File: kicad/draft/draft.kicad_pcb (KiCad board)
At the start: 2 copper layers, 15 parts, among them IC1 LP5024RSMR, J1 Conn_02x05_Odd_Even, U1 NodeMCU2

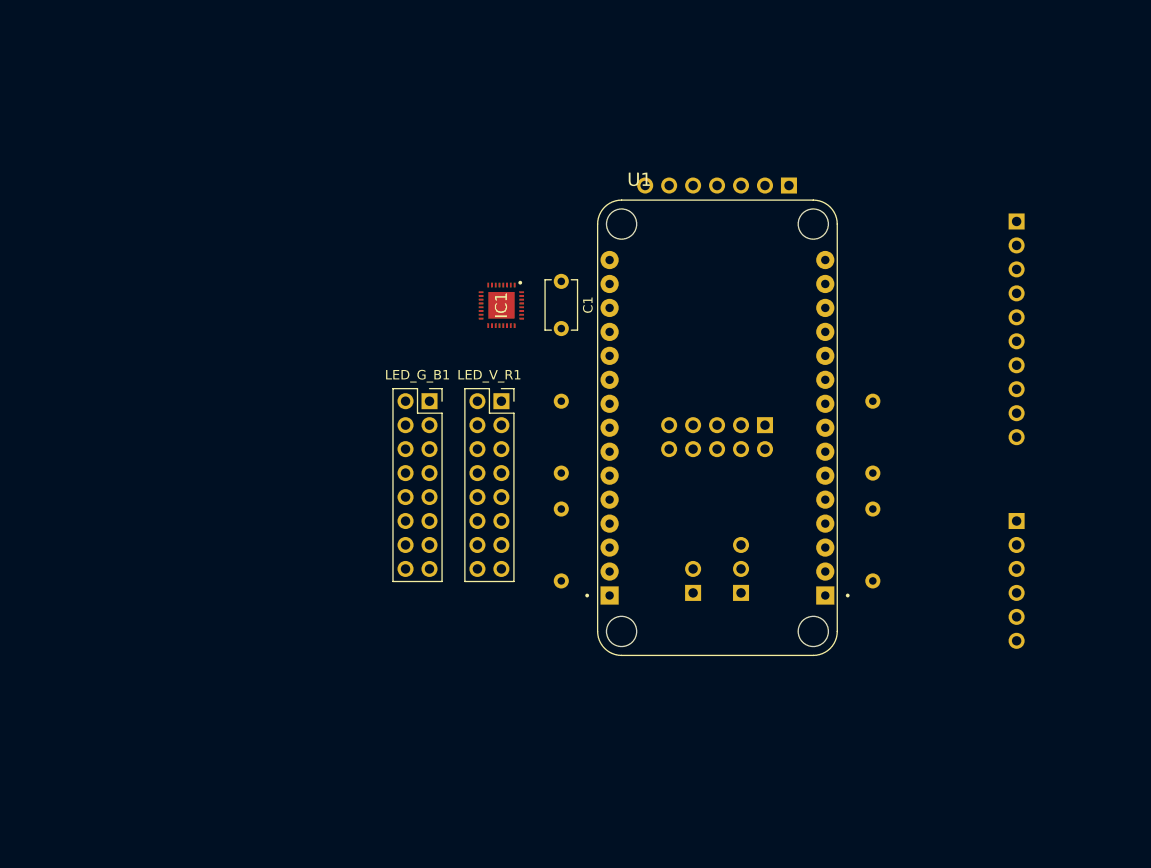
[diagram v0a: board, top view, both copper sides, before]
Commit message: Added GND and 3V3 areas and tracks to connect NodeMCU
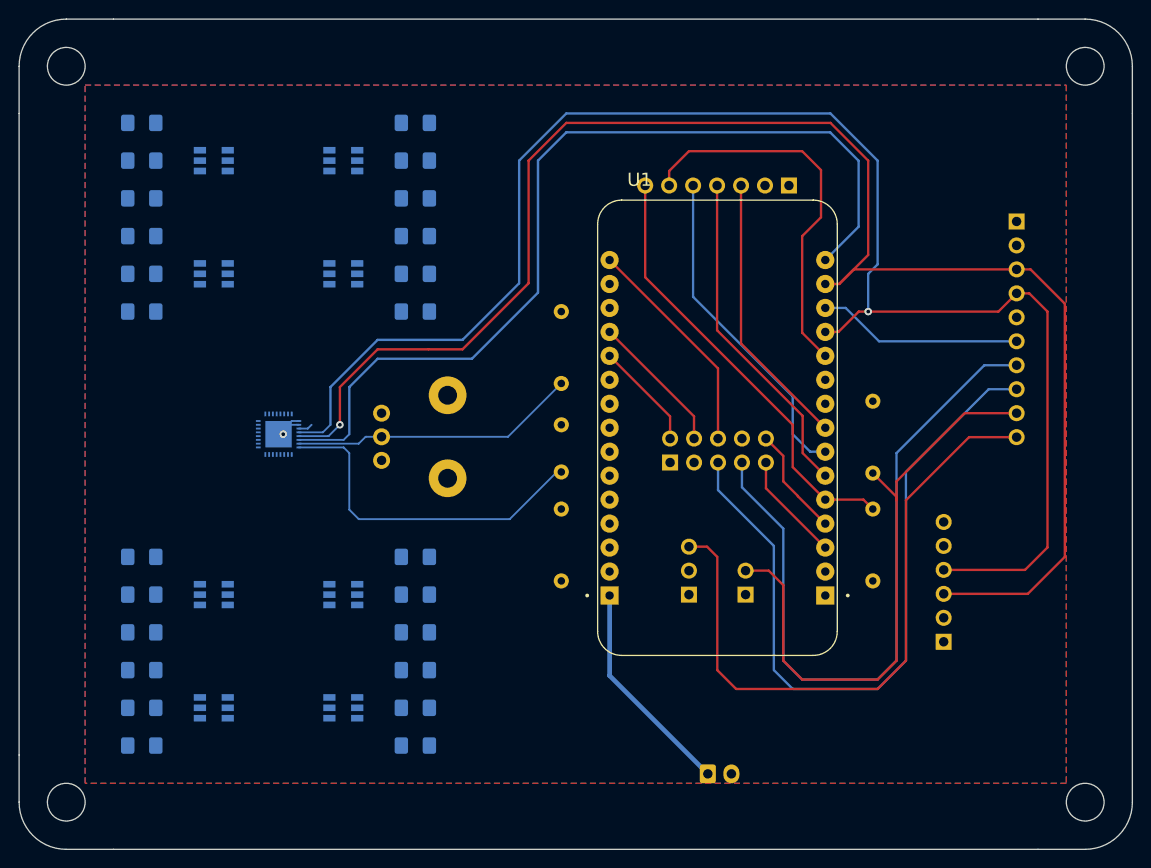
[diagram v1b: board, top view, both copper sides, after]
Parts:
- removed LED_G_B1: LED_G_B, Connector_PinSocket_2.54mm:PinSocket_2x08_P2.54mm_Vertical
- removed LED_V_R1: LED_V_R, Connector_PinSocket_2.54mm:PinSocket_2x08_P2.54mm_Vertical
- added J2: Conn_01x02_Female, Connector_JST:JST_EH_S2B-EH_1x02_P2.50mm_Horizontal, B.Cu at (93.0, 103.0)
- added LED1: LED, SamacSys:KRTBLSLPS132VUVXEQBTBVD8TWTZL1B, B.Cu at (40.6, 38.0)
- added LED2: LED, SamacSys:KRTBLSLPS132VUVXEQBTBVD8TWTZL1B, B.Cu at (40.6, 84.0)
- added LED3: LED, SamacSys:KRTBLSLPS132VUVXEQBTBVD8TWTZL1B, B.Cu at (40.6, 50.0)
- added LED4: LED, SamacSys:KRTBLSLPS132VUVXEQBTBVD8TWTZL1B, B.Cu at (40.6, 96.0)
- added LED5: LED, SamacSys:KRTBLSLPS132VUVXEQBTBVD8TWTZL1B, B.Cu at (54.4, 38.0)
- added LED6: LED, SamacSys:KRTBLSLPS132VUVXEQBTBVD8TWTZL1B, B.Cu at (54.4, 84.0)
- added LED7: LED, SamacSys:KRTBLSLPS132VUVXEQBTBVD8TWTZL1B, B.Cu at (54.4, 50.0)
- added LED8: LED, SamacSys:KRTBLSLPS132VUVXEQBTBVD8TWTZL1B, B.Cu at (54.4, 96.0)
- added R10: 47, Resistor_SMD:R_1206_3216Metric_Pad1.42x1.75mm_HandSolder, B.Cu at (33.0, 92.0)
- added R11: 47, Resistor_SMD:R_1206_3216Metric_Pad1.42x1.75mm_HandSolder, B.Cu at (33.0, 96.0)
- added R12: 100, Resistor_SMD:R_1206_3216Metric_Pad1.42x1.75mm_HandSolder, B.Cu at (33.0, 54.0)
- added R13: 100, Resistor_SMD:R_1206_3216Metric_Pad1.42x1.75mm_HandSolder, B.Cu at (33.0, 100.0)
- added R14: 47, Resistor_SMD:R_1206_3216Metric_Pad1.42x1.75mm_HandSolder, B.Cu at (33.0, 50.0)
- added R15: 47, Resistor_SMD:R_1206_3216Metric_Pad1.42x1.75mm_HandSolder, B.Cu at (33.0, 46.0)
- added R16: 47, Resistor_SMD:R_1206_3216Metric_Pad1.42x1.75mm_HandSolder, B.Cu at (62.0, 88.0)
- added R17: 47, Resistor_SMD:R_1206_3216Metric_Pad1.42x1.75mm_HandSolder, B.Cu at (62.0, 84.0)
- added R18: 100, Resistor_SMD:R_1206_3216Metric_Pad1.42x1.75mm_HandSolder, B.Cu at (62.0, 34.0)
- added R19: 100, Resistor_SMD:R_1206_3216Metric_Pad1.42x1.75mm_HandSolder, B.Cu at (62.0, 80.0)
- added R20: 47, Resistor_SMD:R_1206_3216Metric_Pad1.42x1.75mm_HandSolder, B.Cu at (62.0, 38.0)
- added R21: 47, Resistor_SMD:R_1206_3216Metric_Pad1.42x1.75mm_HandSolder, B.Cu at (62.0, 42.0)
- added R22: 47, Resistor_SMD:R_1206_3216Metric_Pad1.42x1.75mm_HandSolder, B.Cu at (62.0, 100.0)
- added R23: 47, Resistor_SMD:R_1206_3216Metric_Pad1.42x1.75mm_HandSolder, B.Cu at (62.0, 96.0)
- added R24: 100, Resistor_SMD:R_1206_3216Metric_Pad1.42x1.75mm_HandSolder, B.Cu at (62.0, 46.0)
- added R25: 100, Resistor_SMD:R_1206_3216Metric_Pad1.42x1.75mm_HandSolder, B.Cu at (62.0, 92.0)
- added R26: 47, Resistor_SMD:R_1206_3216Metric_Pad1.42x1.75mm_HandSolder, B.Cu at (62.0, 50.0)
- added R27: 47, Resistor_SMD:R_1206_3216Metric_Pad1.42x1.75mm_HandSolder, B.Cu at (62.0, 54.0)
- added R4: 47, Resistor_SMD:R_1206_3216Metric_Pad1.42x1.75mm_HandSolder, B.Cu at (33.0, 80.0)
- added R5: 47, Resistor_SMD:R_1206_3216Metric_Pad1.42x1.75mm_HandSolder, B.Cu at (33.0, 84.0)
- added R6: 100, Resistor_SMD:R_1206_3216Metric_Pad1.42x1.75mm_HandSolder, B.Cu at (33.0, 42.0)
- added R7: 100, Resistor_SMD:R_1206_3216Metric_Pad1.42x1.75mm_HandSolder, B.Cu at (33.0, 88.0)
- added R8: 47, Resistor_SMD:R_1206_3216Metric_Pad1.42x1.75mm_HandSolder, B.Cu at (33.0, 38.0)
- added R9: 47, Resistor_SMD:R_1206_3216Metric_Pad1.42x1.75mm_HandSolder, B.Cu at (33.0, 34.0)
- added RV1: R_POT 5K (for 15mA LED), Potentiometer_THT:Potentiometer_Bourns_PTV09A-1_Single_Vertical, B.Cu at (58.4, 64.8)
- C1, IC1: moved to B.Cu
- moved IC1 27.3 mm to (47.5, 67.0), turned to 90 degrees
- moved C1 20.2 mm to (77.5, 71.0), turned to 90 degrees
- moved R5 17.1 mm to (77.5, 54.0), turned to 270 degrees
- moved BME1 15.0 mm to (118.0, 89.0), turned to 0 degrees
- moved J1 10.8 mm to (89.0, 70.0), turned to 270 degrees
- moved R3 5.56 mm to (97.0, 84.0)
- moved MOIST1 5.52 mm to (91.0, 84.0)
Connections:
- ADC1 pad 10: (no net) -> Net-(ADC1-Pad10)
- ADC1 pad 5: Net-(ADC1-Pad5) -> GND
- C1 pad 1: GND -> Net-(C1-Pad1)
- C1 pad 2: Net-(C1-Pad2) -> GND
- IC1 pad 32: Net-(C1-Pad2) -> Net-(C1-Pad1)
- J1 pad 2: GND -> Net-(J1-Pad2)
- J1 pad 3: Net-(J1-Pad3) -> GND
- J1 pad 5: Net-(J1-Pad5) -> Net-(ADC1-Pad8)
- J1 pad 7: Net-(J1-Pad7) -> Net-(ADC1-Pad7)
- MOIST1 pad 3: Net-(ADC1-Pad6) -> Net-(ADC1-Pad10)
- R2 pad 1: Net-(ADC1-Pad7) -> Net-(ADC1-Pad9)
- R3 pad 2: Net-(ADC1-Pad7) -> Net-(ADC1-Pad9)
- U1 pad A0: Net-(J1-Pad7) -> Net-(J1-Pad6)
- U1 pad D0: Net-(J1-Pad10) -> Net-(IC1-Pad30)
- U1 pad D10: Net-(J1-Pad4) -> Net-(J1-Pad9)
- U1 pad D2: Net-(J1-Pad8) -> Net-(ADC1-Pad6)
- U1 pad D9: Net-(J1-Pad6) -> Net-(J1-Pad10)
- U1 pad SD2: Net-(J1-Pad3) -> Net-(J1-Pad2)
- U1 pad SD3: Net-(J1-Pad5) -> Net-(J1-Pad4)
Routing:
- net Net-(ADC1-Pad3): track 0.00 -> 168.9 mm, vias 0 -> 1
- net Net-(ADC1-Pad4): track 0.00 -> 166.8 mm, vias 0 -> 1
- net Net-(IC1-Pad30): track 0.00 -> 97.2 mm
- net Net-(ADC1-Pad8): track 0.00 -> 75.9 mm
- net Net-(ADC1-Pad7): track 0.00 -> 75.1 mm
- net Net-(ADC1-Pad10): track 0.00 -> 69.0 mm
- net Net-(ADC1-Pad9): track 0.00 -> 65.5 mm
- net Net-(LCD_SPI1-Pad7): track 0.00 -> 46.7 mm
- net Net-(LCD_SPI1-Pad6): track 0.00 -> 40.9 mm
- net Net-(C1-Pad1): track 0.00 -> 36.6 mm
- net Net-(LCD_SPI1-Pad4): track 0.00 -> 35.5 mm
- net Net-(LCD_SPI1-Pad5): track 0.00 -> 35.0 mm
- net Net-(IC1-Pad31): track 0.00 -> 30.5 mm
- net Net-(LCD_SPI1-Pad3): track 0.00 -> 29.4 mm
- net Net-(J1-Pad6): track 0.00 -> 23.7 mm
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- added copper zone on B.Cu, net +3V3
- added copper zone on F.Cu, net GND
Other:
- board outline added: 118 x 88 mm
- net class IC_LD_OUT added: clearance 0.1, trace_width 0.2, via_dia 0.8, via_drill 0.4

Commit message: PCB 0.1 sent to production
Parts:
- removed the R4 at (33.0, 80.0)
- removed the R4 at (77.5, 82.5)
- removed the R5 at (33.0, 84.0)
- removed the R5 at (77.5, 54.0)
- added C2: 1μF, Capacitor_SMD:C_1206_3216Metric_Pad1.42x1.75mm_HandSolder, B.Cu at (59.1, 62.2)
- added R4: 47, Resistor_SMD:R_1206_3216Metric_Pad1.42x1.75mm_HandSolder, B.Cu at (40.0, 80.0)
- added R5: 47, Resistor_SMD:R_1206_3216Metric_Pad1.42x1.75mm_HandSolder, B.Cu at (40.0, 84.0)
- C1: footprint Capacitor_THT:C_Disc_D5.1mm_W3.2mm_P5.00mm -> Capacitor_SMD:C_1206_3216Metric_Pad1.42x1.75mm_HandSolder
- R1, R2: footprint Resistor_THT:R_Axial_DIN0207_L6.3mm_D2.5mm_P7.62mm_Horizontal -> Resistor_SMD:R_1206_3216Metric_Pad1.42x1.75mm_HandSolder
- moved C1 18.4 mm to (59.1, 71.8), turned to 0 degrees
- moved LED6 13.9 mm to (61.3, 96.0)
- moved LED8 13.9 mm to (61.3, 84.0)
- moved R16 13.9 mm to (69.0, 100.0)
- moved R17 13.9 mm to (69.0, 96.0)
- moved R19 13.9 mm to (69.0, 92.0)
- moved R22 13.9 mm to (69.0, 88.0)
- moved R23 13.9 mm to (69.0, 84.0)
- moved R25 13.9 mm to (69.0, 80.0)
- moved R1 10.4 mm to (110.5, 72.2), turned to 270 degrees
- moved IC1 6.98 mm to (54.5, 67.0)
- moved LED1 6.98 mm to (47.6, 38.0)
- moved LED2 6.98 mm to (47.6, 84.0)
- moved LED3 6.98 mm to (47.6, 50.0)
- moved LED4 6.98 mm to (47.6, 96.0)
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- renumbered R3 to PHOTO1
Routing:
- net Net-(IC1-Pad16): track 0.00 -> 34.1 mm
- net GND: track 5.29 -> 38.3 mm, vias 1 -> 4
- net Net-(IC1-Pad15): track 0.00 -> 32.9 mm
- net Net-(IC1-Pad17): track 0.00 -> 32.9 mm
- net Net-(IC1-Pad14): track 0.00 -> 32.8 mm
- net Net-(C1-Pad1): track 36.6 -> 3.74 mm
- net Net-(IC1-Pad13): track 0.00 -> 31.2 mm
- net Net-(IC1-Pad6): track 0.00 -> 30.7 mm
- net Net-(IC1-Pad7): track 0.00 -> 30.3 mm
- net Net-(IC1-Pad18): track 0.00 -> 30.2 mm
- net Net-(IC1-Pad5): track 0.00 -> 29.7 mm
- net Net-(IC1-Pad8): track 0.00 -> 28.8 mm
- net Net-(IC1-Pad4): track 0.00 -> 27.9 mm
- net Net-(IC1-Pad9): track 0.00 -> 27.8 mm
- net Net-(IC1-Pad31): track 30.5 -> 9.07 mm
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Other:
- net class IC_LD_OUT: clearance 0.1 -> 0.2
